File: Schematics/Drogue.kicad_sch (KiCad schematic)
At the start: 6 parts, among them J4 Drouge, Q2 IRLML2502TRPBF

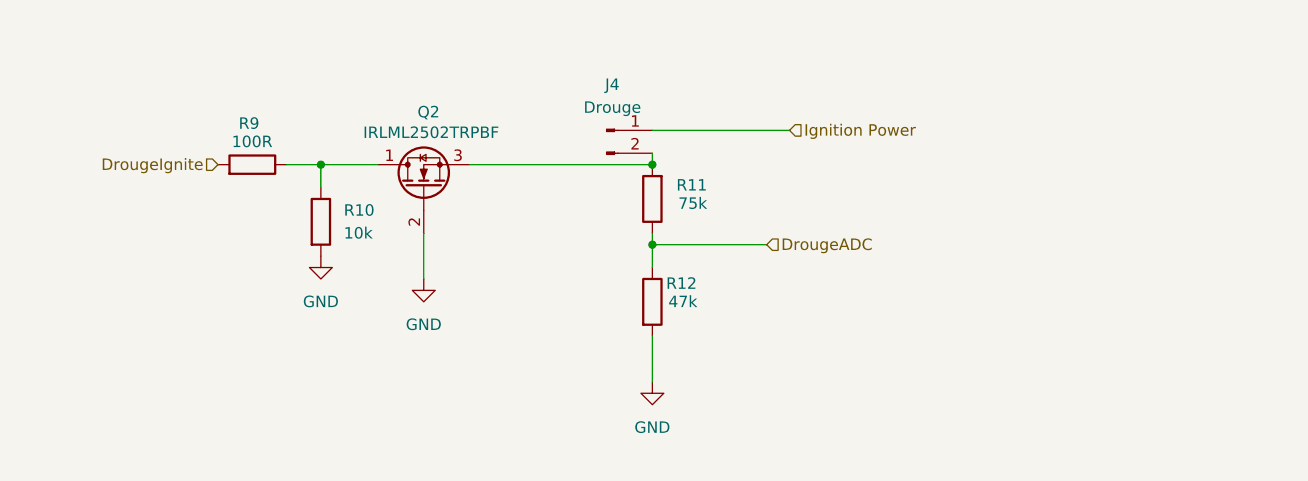
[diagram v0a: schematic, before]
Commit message: layout completed added testpoints and verified mosfet ect
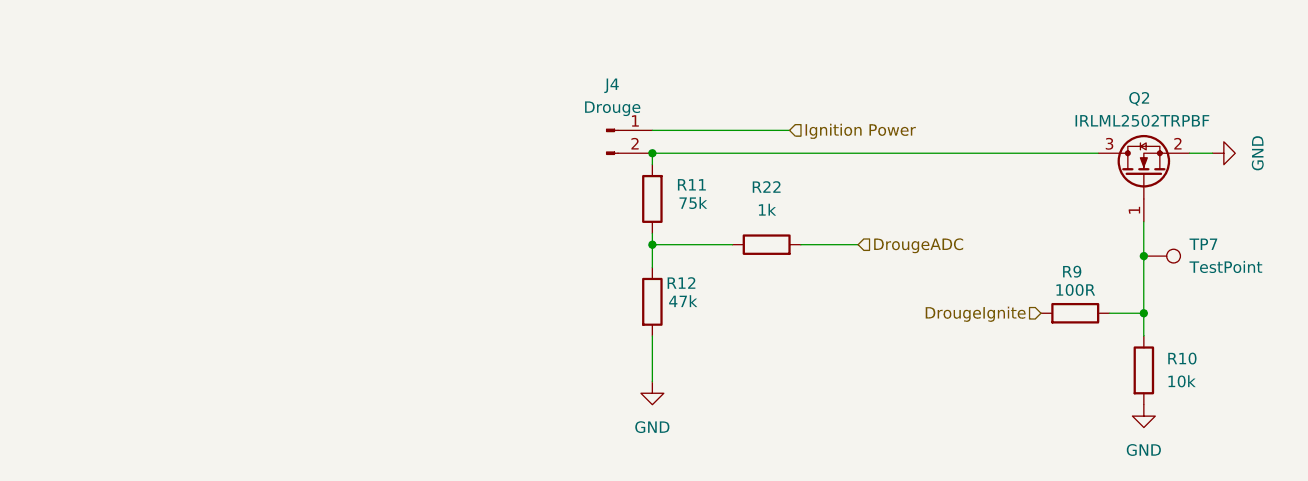
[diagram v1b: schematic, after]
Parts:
- added R22: 1k, Resistor_SMD:R_0805_2012Metric_Pad1.20x1.40mm_HandSolder, symbol Device:R
- added TP7: TestPoint, TestPoint:TestPoint_Pad_1.5x1.5mm, symbol Connector:TestPoint
- Q2: symbol Transistor_FET:Q_NMOS_DGS -> Transistor_FET:Q_NMOS_GSD
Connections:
- net DrougeADC: now also R22.2; no longer R11.1, R12.1
- net at Q2.1 (G), R10.1, R9.1: now also TP7.1
- new net: R11.1, R12.1, R22.1
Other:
- moved on the sheet: Q2, R10, R9

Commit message: added comments, awaiting review
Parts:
- R22: LCSC (none) -> C95781
- TP7: now left out of the parts list
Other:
- note added: "Continuity detection with adc resistors to protect adc pins"
- note added: "Low-Side Mosfet Switch for pulling igniton to ground"
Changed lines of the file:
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@@
 	(generator_version "9.0")
 	(paper "A4")
+	(text "Continuity detection with adc resistors to protect adc pins"
+		(exclude_from_sim no)
+		(at 98.298 91.44 0)
+		(effects
+			(font
+				(size 1.27 1.27)
+			)
+		)
+	)
+	(text "Low-Side Mosfet Switch for pulling igniton to ground"
+		(exclude_from_sim no)
+		(at 156.972 64.008 0)
+		(effects
+			(font
+				(size 1.27 1.27)
+			)
+		)
+	)
 	(junction
 		(at 187.96 95.25)
@@
 		(unit 1)
 		(exclude_from_sim no)
-		(in_bom yes)
+		(in_bom no)
 		(on_board yes)
 		(dnp no)
@@
 			(effects
 				(font
+					(size 1.27 1.27)
+				)
+				(hide yes)
+			)
+		)
+		(property "LCSC" "C95781"
+			(at 146.05 87.63 90)
+			(effects
+				(font

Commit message: updated to KiCad 10.0, updated .gitignore
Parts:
- R10: LCSC C84376 -> C17414
- R12: LCSC C2933415 -> C17713
- R22: LCSC C95781 -> C17513
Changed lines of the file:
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@@
 			)
 		)
-		(property "LCSC" "C84376"
+		(property "LCSC" "C17414"
 			(at 187.96 101.6 0)
 			(effects
@@
 			)
 		)
-		(property "LCSC" "C2933415"
+		(property "LCSC" "C17713"
 			(at 133.35 93.98 0)
 			(effects
@@
 			)
 		)
-		(property "LCSC" "C95781"
+		(property "LCSC" "C17513"
 			(at 146.05 87.63 90)
 			(effects
